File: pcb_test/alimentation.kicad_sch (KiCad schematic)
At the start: 11 parts, among them SW1 SW_SPST, U3 PTPSM861253RDXR

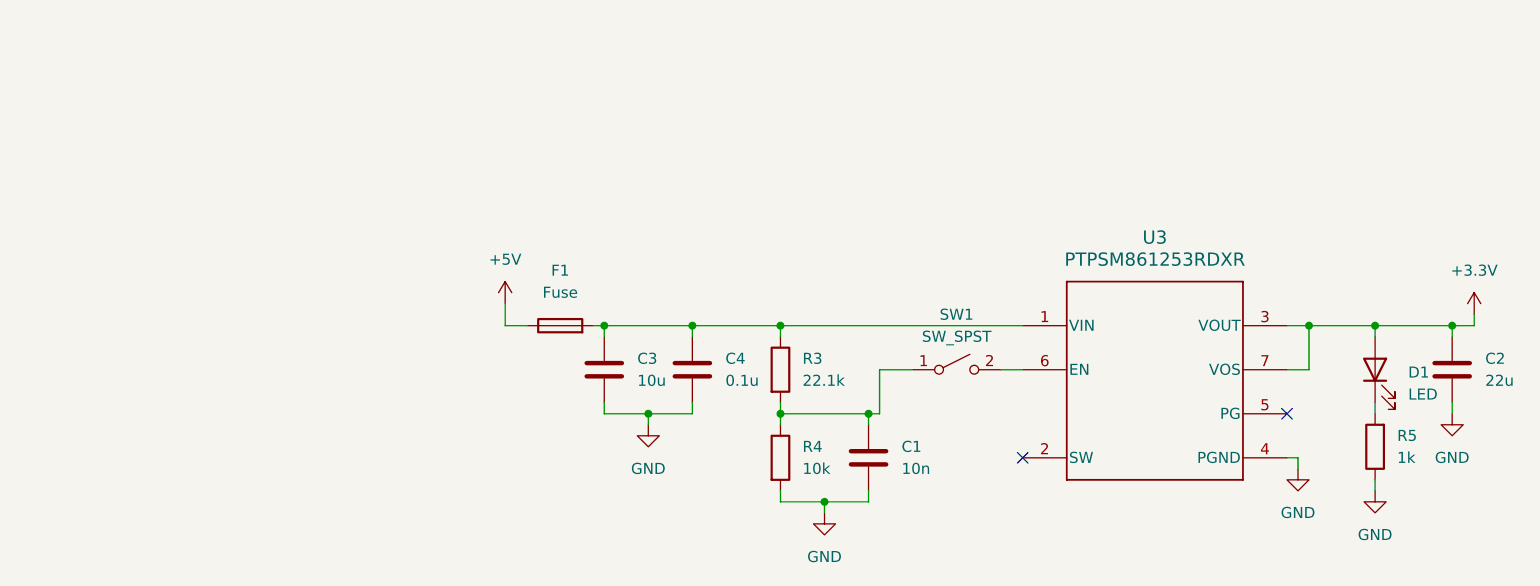
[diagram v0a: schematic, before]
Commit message: Ajout GPS, retrait radio, clean up schemas
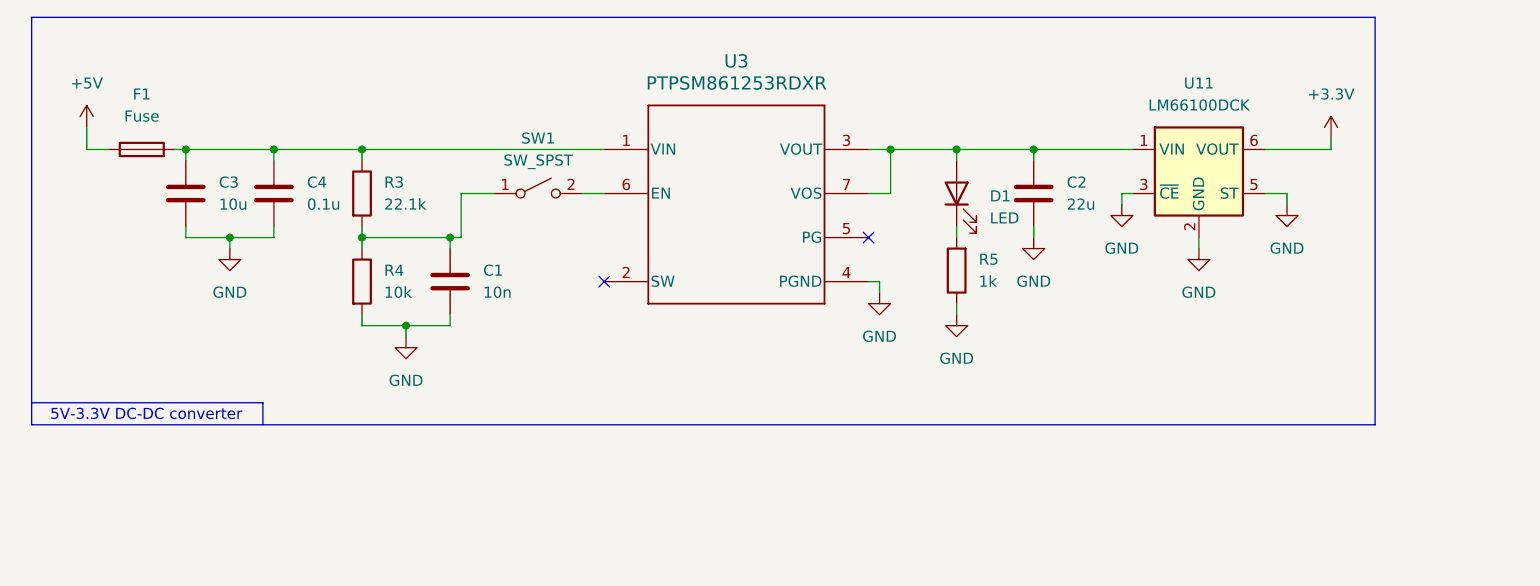
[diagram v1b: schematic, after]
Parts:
- added U11: LM66100DCK, Package_TO_SOT_SMD:SOT-363_SC-70-6, symbol Power_Management:LM66100DCK
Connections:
- net +3.3V: now also U11.6 (VOUT); no longer C2.1, D1.2 (A), U3.3 (VOUT), U3.7 (VOS)
- net GND: now also U11.2 (GND), U11.3 (~{CE}), U11.5 (ST)
- new net: C2.1, D1.2 (A), U11.1 (VIN), U3.3 (VOUT), U3.7 (VOS)
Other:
- note added: "5V-3.3V DC-DC converter"
- moved on the sheet: C1, C2, C3, C4, D1, F1, R3, R4, R5, SW1, U3

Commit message: Ajout testpoints
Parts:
- added TP1, TP2, TP3, TP6: TestPoint, symbol Connector:TestPoint
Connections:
- net +3.3V: now also TP2.1
- net +5V: now also TP3.1
- net GND: now also TP6.1
- net 3V3_Vout: now reaches C2.1, D1.2 (A), U11.1 (VIN), U3.3 (VOUT), U3.7 (VOS)
- net 3V3_Vout: now also TP1.1

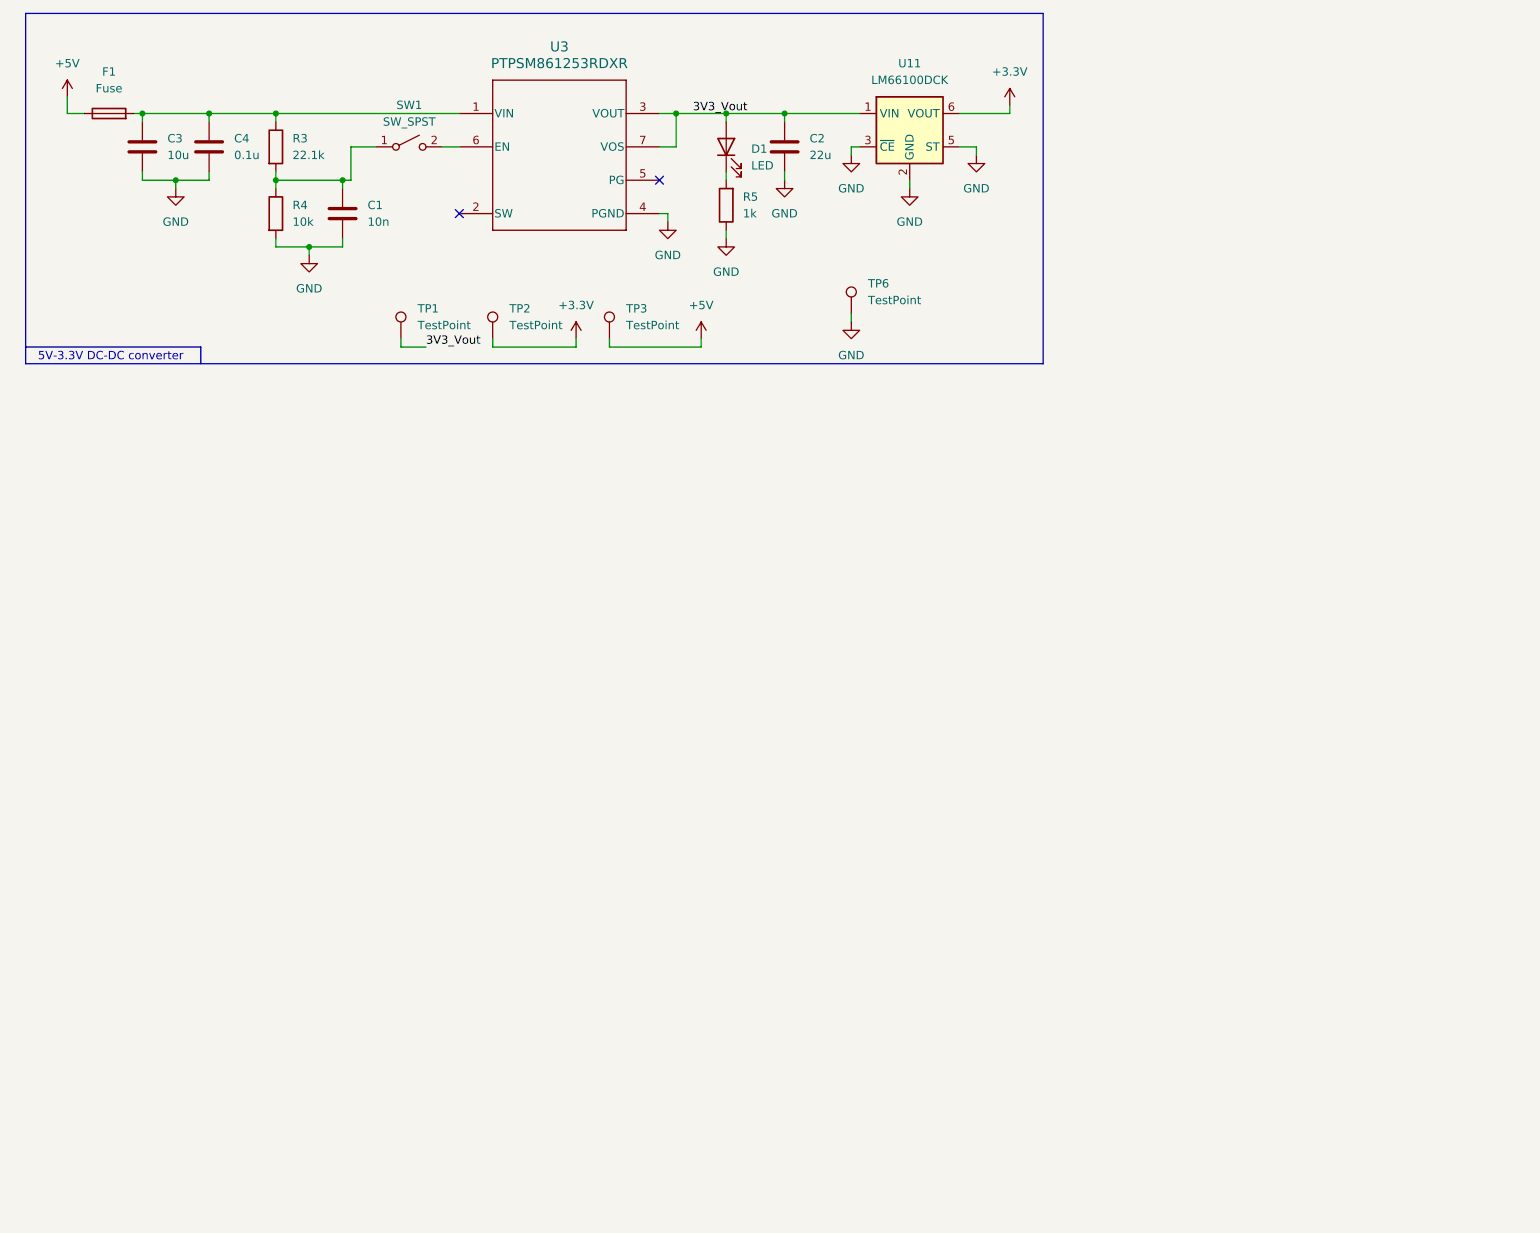
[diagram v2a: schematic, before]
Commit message: refait alimentation, changement MCU, separation schema eMMC/octospi, reajout RF
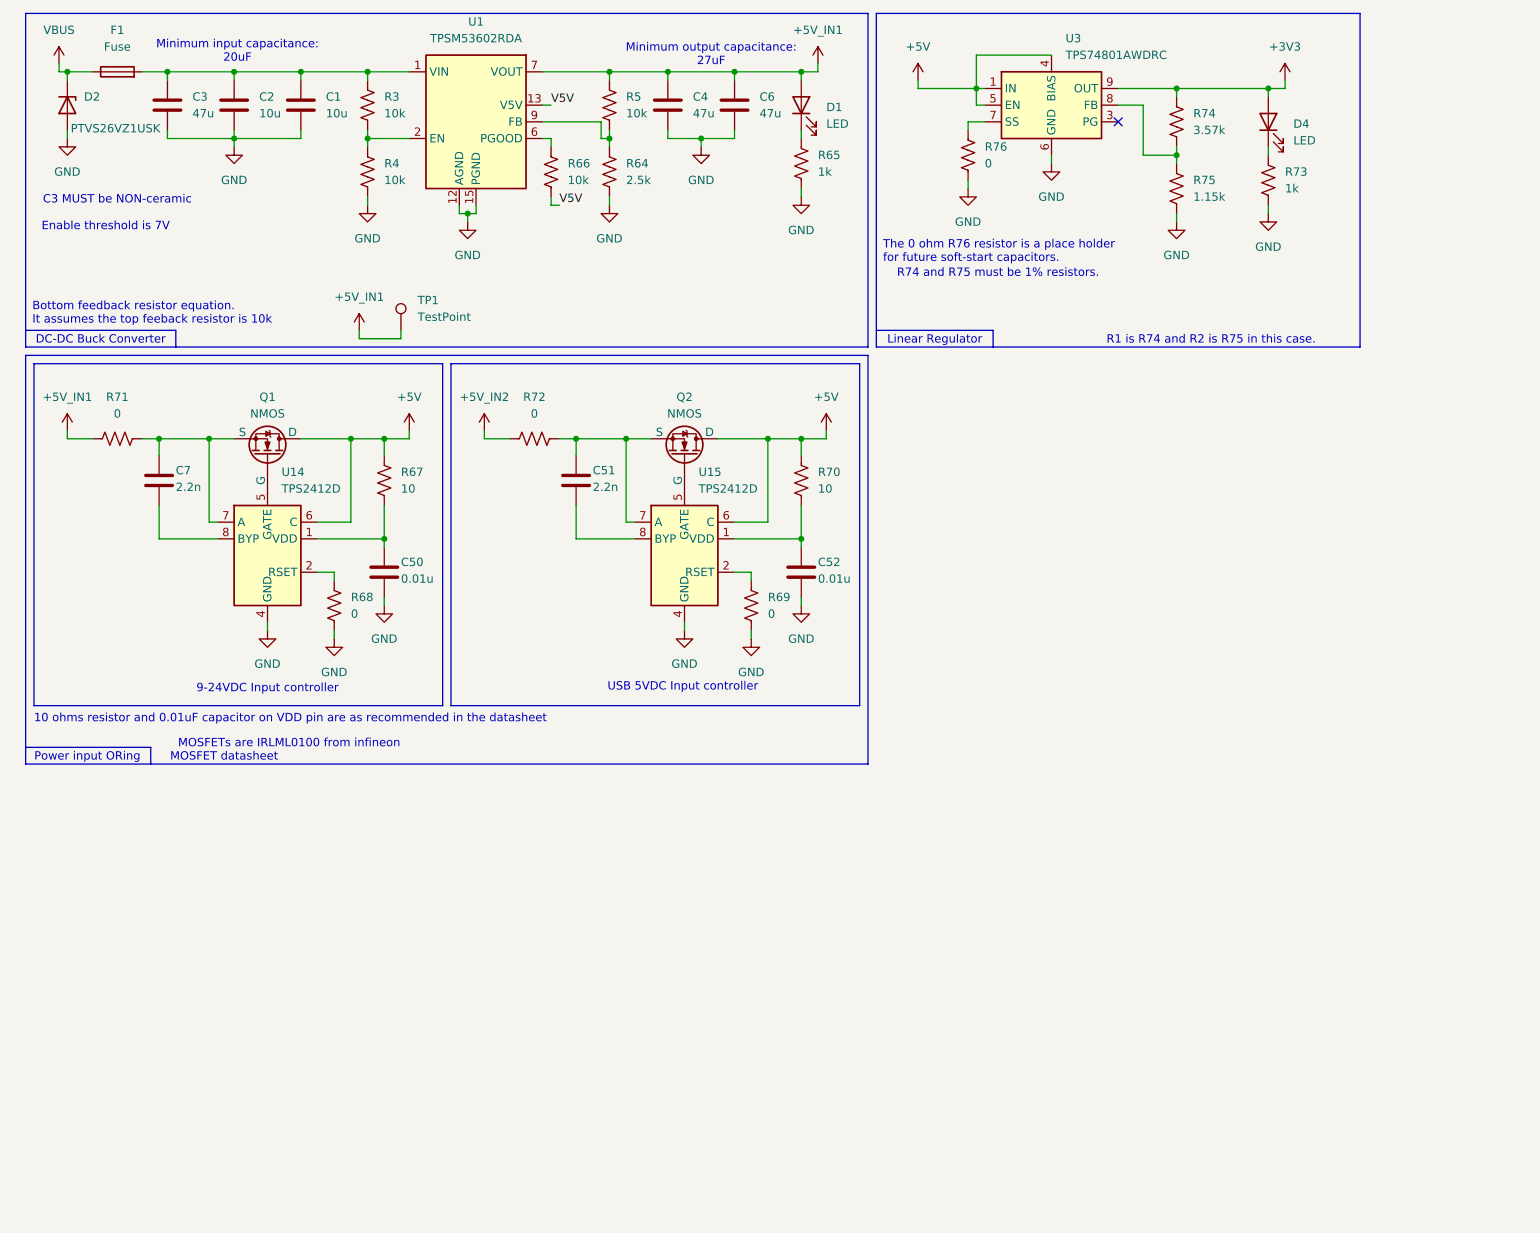
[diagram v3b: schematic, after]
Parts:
- removed R3: 22.1k, symbol Device:R
- removed R4: 10k, symbol Device:R
- removed R5: 1k, symbol Device:R
- removed SW1: SW_SPST, symbol Switch:SW_SPST
- removed TP2, TP3, TP6: TestPoint, symbol Connector:TestPoint
- removed U11: LM66100DCK, Package_TO_SOT_SMD:SOT-363_SC-70-6, symbol Power_Management:LM66100DCK
- removed U3: PTPSM861253RDXR, TPSM861253:RDX0007A-MFG, symbol TPSM861253:PTPSM861253RDXR
- added C50, C52: 0.01u, symbol Device:C
- added C51, C7: 2.2n, symbol Device:C
- added C6: 47u, symbol Device:C
- added D2: PTVS26VZ1USK, Diode_SMD:Nexperia_DSN1608-2_1.6x0.8mm, symbol Diode:PTVS26VZ1USK
- added D4: LED, symbol Device:LED
- added Q1, Q2: NMOS, symbol Simulation_SPICE:NMOS
- added R3, R4, R5, R66: 10k, symbol Device:R_US
- added R64: 2.5k, symbol Device:R_US
- added R65, R73: 1k, symbol Device:R_US
- added R67, R70: 10, symbol Device:R_US
- added R68, R69, R71, R72, R76: 0, symbol Device:R_US
- added R74: 3.57k, symbol Device:R_US
- added R75: 1.15k, symbol Device:R_US
- added U1: TPSM53602RDA, Package_DFN_QFN:Texas_B3QFN-14-1EP_5x5.5mm_P0.65mm_ThermalVia, symbol Converter_DCDC:TPSM53602RDA
- added U14, U15: TPS2412D, symbol Power_Management:TPS2412D
- added U3: TPS74801AWDRC, Package_SON:VSON-10-1EP_3x3mm_P0.5mm_EP1.65x2.4mm_ThermalVias, symbol Regulator_Linear:TPS74801AWDRC
- C1: value 10n -> 10u
- C2: value 22u -> 10u
- C3: value 10u -> 47u
- C4: value 0.1u -> 47u
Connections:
- net +5V: now also Q1.1 (D), Q2.1 (D), R67.1, R70.1, U14.6 (C), U15.6 (C), U3.1 (IN), U3.2 (IN), U3.4 (BIAS), U3.5 (EN); no longer F1.1
- net GND: now also C50.2, C52.2, C6.2, D2.2 (A), R4.2, R64.2, R65.2, R68.2, R69.2, R73.2, R75.2, R76.2, U1.10 (PGND), U1.11 (PGND), U1.12 (AGND), U1.15 (PGND), U1.3 (PGND), U14.3 (GND), U14.4 (GND), U15.3 (GND), U15.4 (GND), U3.11 (GND), U3.6 (GND)
- net at C1.1: now also C2.1, C3.1, F1.2, R3.1, U1.1 (VIN), U1.14 (VIN)
- net at D1.1 (K): now also R65.1
- net 3V3_Vout renamed +5V_IN1
- net +5V_IN1: now also C4.1, C6.1, R5.1, R71.1, U1.7 (VOUT), U1.8 (VOUT); no longer C2.1
- new net: Q2.2 (G), U15.5 (GATE)
- new net: C51.1, Q2.3 (S), R72.2, U15.7 (A)
- new net: C7.1, Q1.3 (S), R71.2, U14.7 (A)
- new net: C7.2, U14.8 (BYP)
- new net: Q1.2 (G), U14.5 (GATE)
- new net: C51.2, U15.8 (BYP)
- new net: C50.1, R67.2, U14.1 (VDD)
- new net: R74.2, R75.1, U3.8 (FB)
- new net: R68.1, U14.2 (RSET)
- new net: R3.2, R4.1, U1.2 (EN)
- new net: R66.1, U1.6 (PGOOD)
- new net: R5.2, R64.1, U1.9 (FB)
- new net: R76.1, U3.7 (SS)
- new net: D4.1 (K), R73.1
- new net: C52.1, R70.2, U15.1 (VDD)
- new net: R69.1, U15.2 (RSET)
- new net +3V3: D4.2 (A), R74.1, U3.10 (OUT), U3.9 (OUT)
- new net +5V_IN2: R72.1
- new net V5V: R66.2, U1.13 (V5V)
- new net VBUS: D2.1 (K), F1.1
- no-connect marks 2 -> 1
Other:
- note added: "10 ohms resistor and 0.01uF capacitor on VDD pin are as recommended in the datasheet"
- note added: "9-24VDC Input controller"
- note added: "Bottom feedback resistor equation. It assumes the top feeback resistor is 10k"
- note added: "C3 MUST be NON-ceramic"
- note added: "DC-DC Buck Converter"
- note added: "Enable threshold is 7V"
- note added: "Linear Regulator"
- note added: "MOSFET datasheet"
- note added: "MOSFETs are IRLML0100 from infineon"
- note added: "Minimum input capacitance: 20uF"
- note added: "Minimum output capacitance: 27uF"
- note added: "Power input ORing"
- note added: "R1 is R74 and R2 is R75 in this case."
- note added: "R74 and R75 must be 1% resistors."
- note added: "The 0 ohm R76 resistor is a place holder for future soft-start capacitors."
- note added: "USB 5VDC Input controller"
- note removed: "5V-3.3V DC-DC converter"

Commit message: alimentation finale. Retouches testpoints et condo decouplage, finalisation requis, ajout sheet finale.
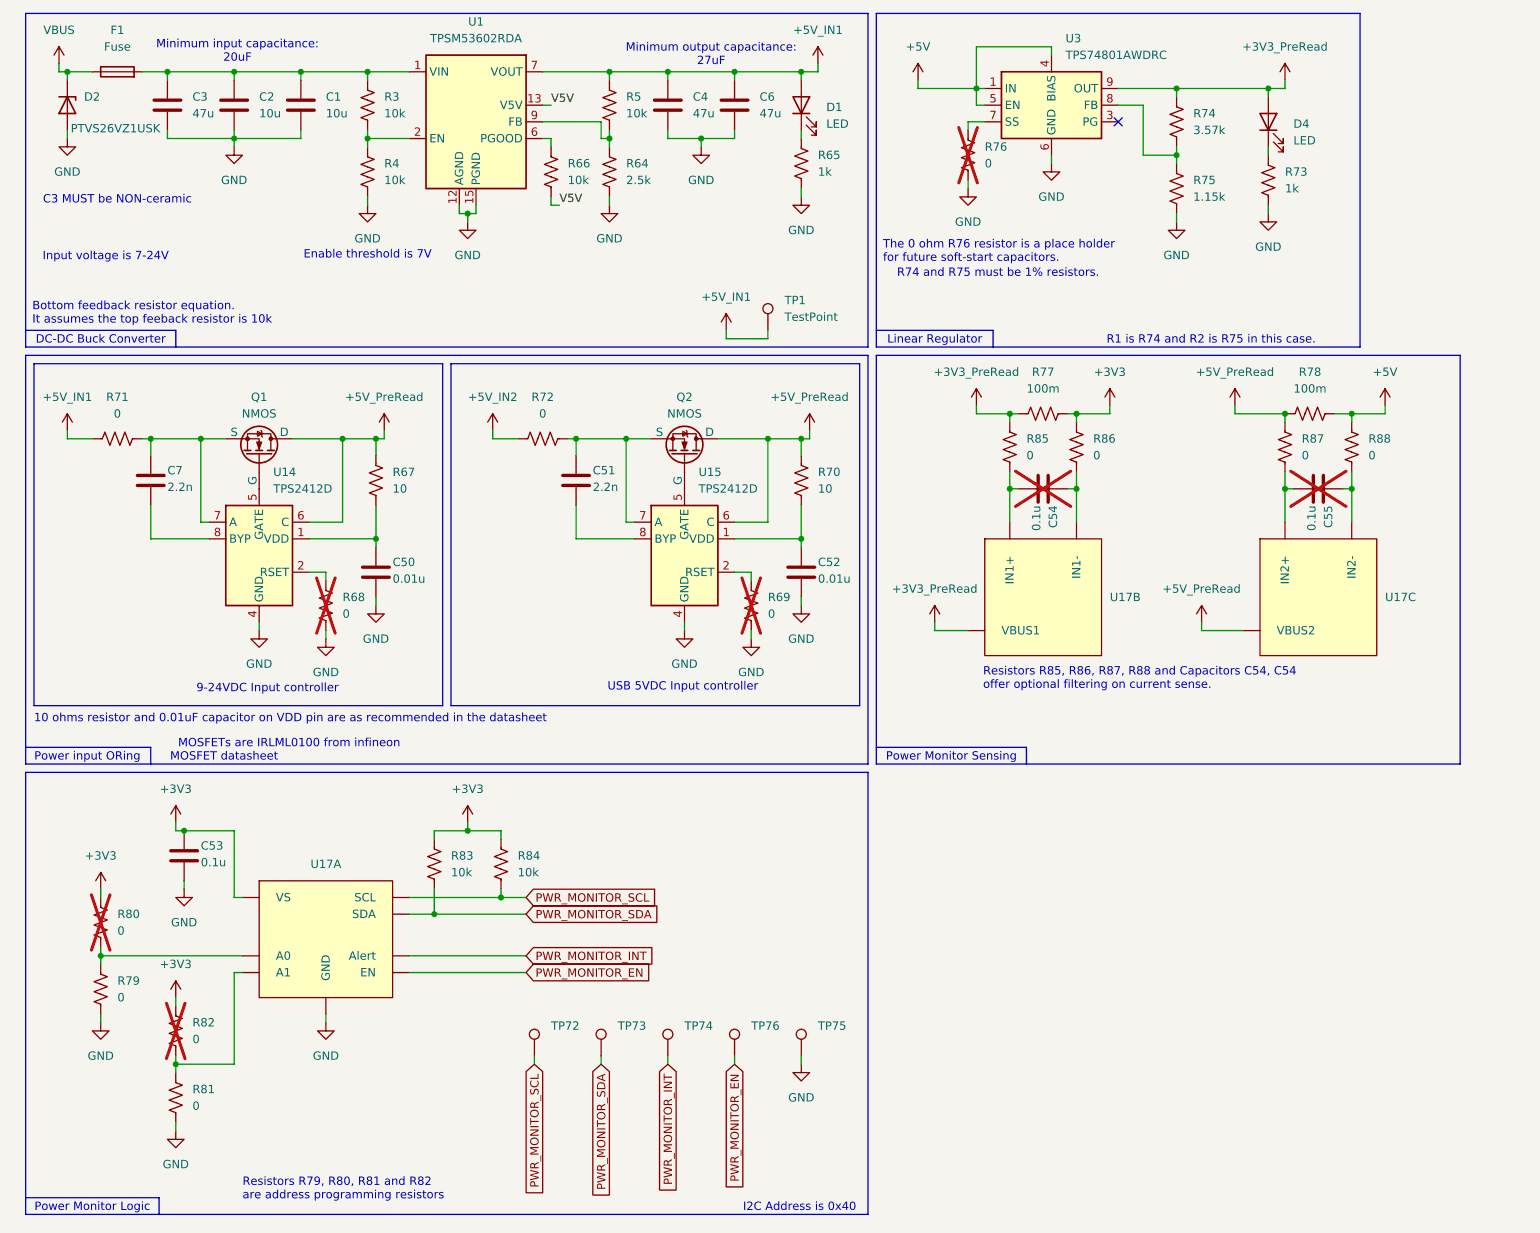
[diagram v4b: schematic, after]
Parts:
- added C53, C54, C55: 0.1u, symbol Device:C
- added R77, R78: 100m, symbol Device:R_US
- added R79, R80, R81, R82, R85, R86, R87, R88: 0, symbol Device:R_US
- added R83, R84: 10k, symbol Device:R_US
- added TP72, TP73, TP74, TP75, TP76: TestPoint, symbol Connector:TestPoint
- added U17: (no value), symbol stuff:INA2227
- R68, R69, R76: now not fitted
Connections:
- net +3V3: now also C53.1, R77.2, R80.2, R82.2, R83.2, R84.2, R86.2, U17. (EN); no longer D4.2 (A), R74.1, U3.10 (OUT), U3.9 (OUT)
- net +5V: now also R78.2, R88.2; no longer Q1.1 (D), Q2.1 (D), R67.1, R70.1, U14.6 (C), U15.6 (C)
- net GND: now also C53.2, R79.1, R81.1, TP75.1, U17. (EN)
- new net: C54.1, R86.1, U17. (IN1-)
- new net: C54.2, R85.1, U17. (IN1-)
- new net: C55.1, R88.1, U17. (IN2-)
- new net: C55.2, R87.1, U17. (IN2-)
- new net: R79.2, R80.1, U17. (EN)
- new net: R81.2, R82.1, U17. (EN)
- new net +3V3_PreRead: D4.2 (A), R74.1, R77.1, R85.2, U17. (IN1-), U3.10 (OUT), U3.9 (OUT)
- new net +5V_PreRead: Q1.1 (D), Q2.1 (D), R67.1, R70.1, R78.1, R87.2, U14.6 (C), U15.6 (C), U17. (IN2-)
- new net PWR_MONITOR_EN: TP76.1, U17. (EN)
- new net PWR_MONITOR_INT: TP74.1, U17. (EN)
- new net PWR_MONITOR_SCL: R84.1, TP72.1, U17. (EN)
- new net PWR_MONITOR_SDA: R83.1, TP73.1, U17. (EN)
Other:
- note added: "I2C Address is 0x40"
- note added: "Input voltage is 7-24V"
- note added: "Power Monitor Logic"
- note added: "Power Monitor Sensing"
- note added: "Resistors R79, R80, R81 and R82 are address programming resistors"
- note added: "Resistors R85, R86, R87, R88 and Capacitors C54, C54 offer optional filtering on current sense."
- moved on the sheet: C50, C7, Q1, R67, R72, TP1, U14
